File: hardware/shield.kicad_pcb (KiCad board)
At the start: 2 copper layers, 50 parts, among them P1 D0_7, P10 CONN_1, P11 CONN_1, P12 CONN_1, P13 CONN_1, P14 CONN_1, P15 CONN_1, P16 CONN_1, P17 CONN_1, P18 CONN_1, P19 P5v, P2 D8_13, P20 EXT1, P21 ADDR_EXT, P22 EXT2, P3 POWER, P4 A0_5, P5 POWER, P6 BOARD, P7 CONN_1, P8 CONN_1, P9 CONN_1, Q1 MOS_P, Q2 MOS_P, Q3 MOS_P, Q4 MOS_P, Q5 MOS_P, Q6 MOS_P, Q7 MOS_P, Q8 MOS_P, U1 74HCT138

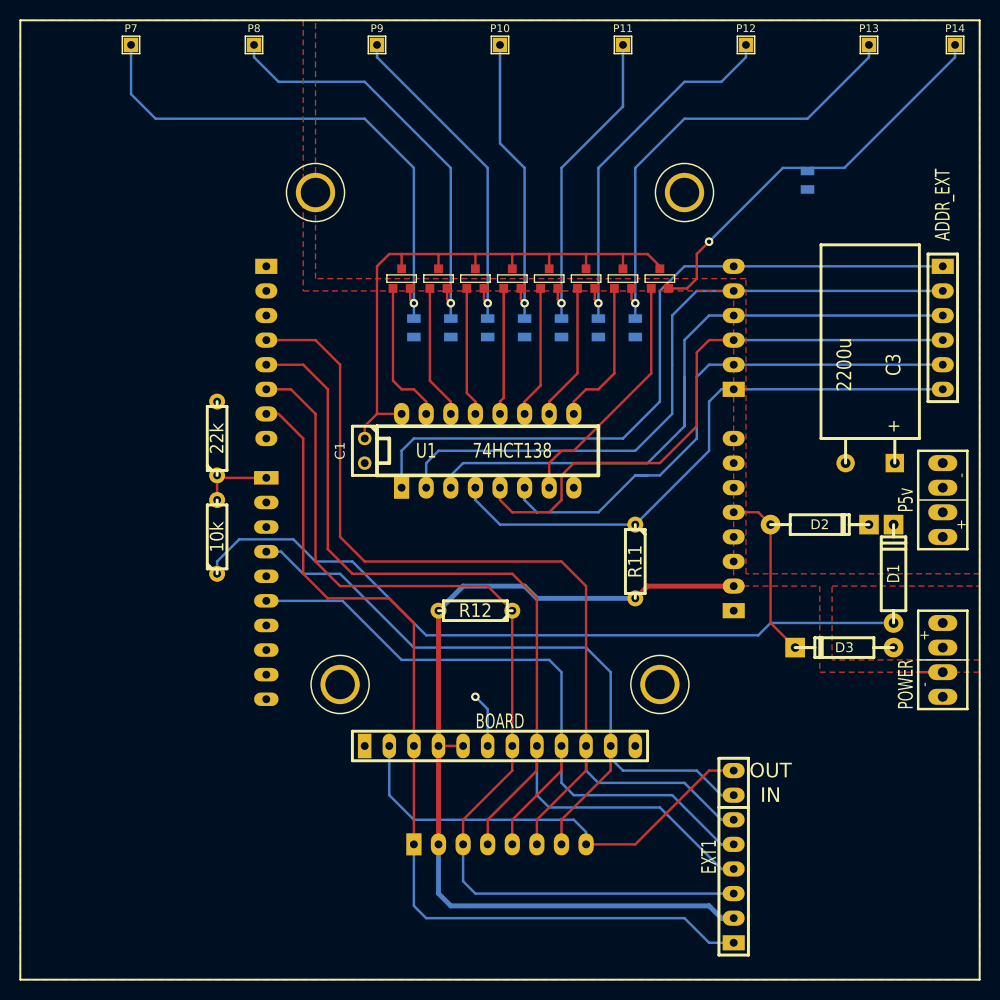
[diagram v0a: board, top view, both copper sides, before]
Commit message: Fix anode mosfet orientation
Signed-off-by: Paul Brook <paul@nowt.org>
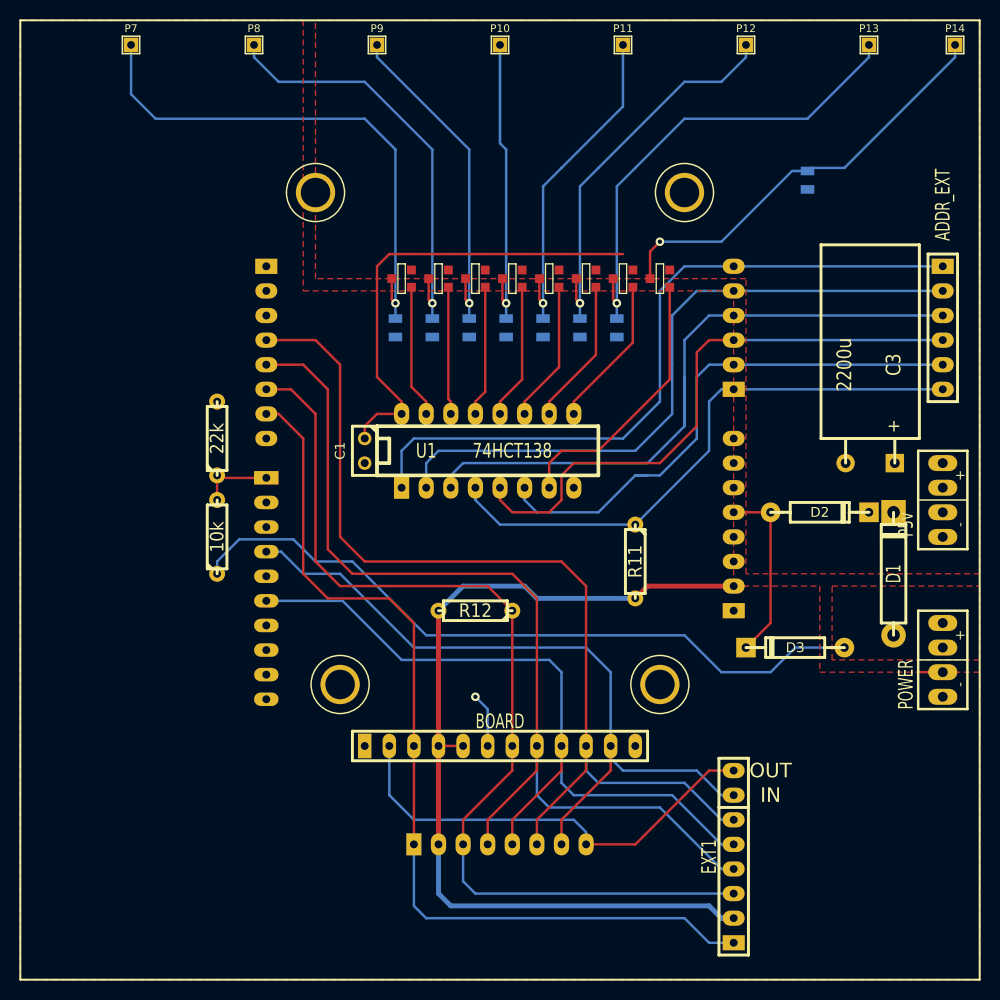
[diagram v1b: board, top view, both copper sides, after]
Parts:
- D1: footprint D4 -> D5
- moved D3 5.08 mm to (106.7, 91.4)
- moved R1 1.91 mm to (65.4, 58.4)
- moved R2 1.91 mm to (69.2, 58.4)
- moved R3 1.91 mm to (73.0, 58.4)
- moved R4 1.91 mm to (76.8, 58.4)
- moved R5 1.91 mm to (80.6, 58.4)
- moved R6 1.91 mm to (84.5, 58.4)
- moved R7 1.91 mm to (88.3, 58.4)
- moved D2 1.27 mm to (109.2, 77.5)
- turned P19 to 90 degrees
- turned Q1 to 270 degrees
- turned Q2 to 270 degrees
- turned Q3 to 270 degrees
- turned Q4 to 270 degrees
- turned Q5 to 270 degrees
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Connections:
- Q1 pad D: /5v -> /S1
- Q1 pad S: /S1 -> /5v
- Q2 pad D: /5v -> /S2
- Q2 pad S: /S2 -> /5v
- Q3 pad D: /5v -> /S3
- Q3 pad S: /S3 -> /5v
- Q4 pad D: /5v -> /S4
- Q4 pad S: /S4 -> /5v
- Q5 pad D: /5v -> /S5
- Q5 pad S: /S5 -> /5v
- Q6 pad D: /5v -> /S6
- Q6 pad S: /S6 -> /5v
- Q7 pad D: /5v -> /S7
- Q7 pad S: /S7 -> /5v
- Q8 pad D: /5v -> /S8
- Q8 pad S: /S8 -> /5v
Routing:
- net /5v: track 62.0 -> 47.8 mm
- net /5v_EXT: track 76.7 -> 73.7 mm
- net /Q8: track 25.7 -> 28.1 mm
- net /S7: track 47.4 -> 49.2 mm
- net /S6: track 38.5 -> 40.3 mm
- net /S5: track 32.6 -> 34.4 mm
- net /Q1: track 15.1 -> 13.7 mm
- net /S8: track 42.5 -> 43.9 mm
- net /Q5: track 13.6 -> 14.6 mm
- net /Q6: track 14.2 -> 15.1 mm
- net /Q4: track 13.1 -> 14.0 mm
- net /5v_USB: track 18.1 -> 18.8 mm
- net /Q2: track 13.8 -> 13.2 mm
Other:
- board text added: "A0"
- board text added: "A1"
- board text added: "A2"
- board text added: "A3"
- board text added: "A3in"
- board text added: "A_En"
